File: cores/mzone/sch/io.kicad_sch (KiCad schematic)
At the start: 88 parts, among them SW3 SW_DIP_x06

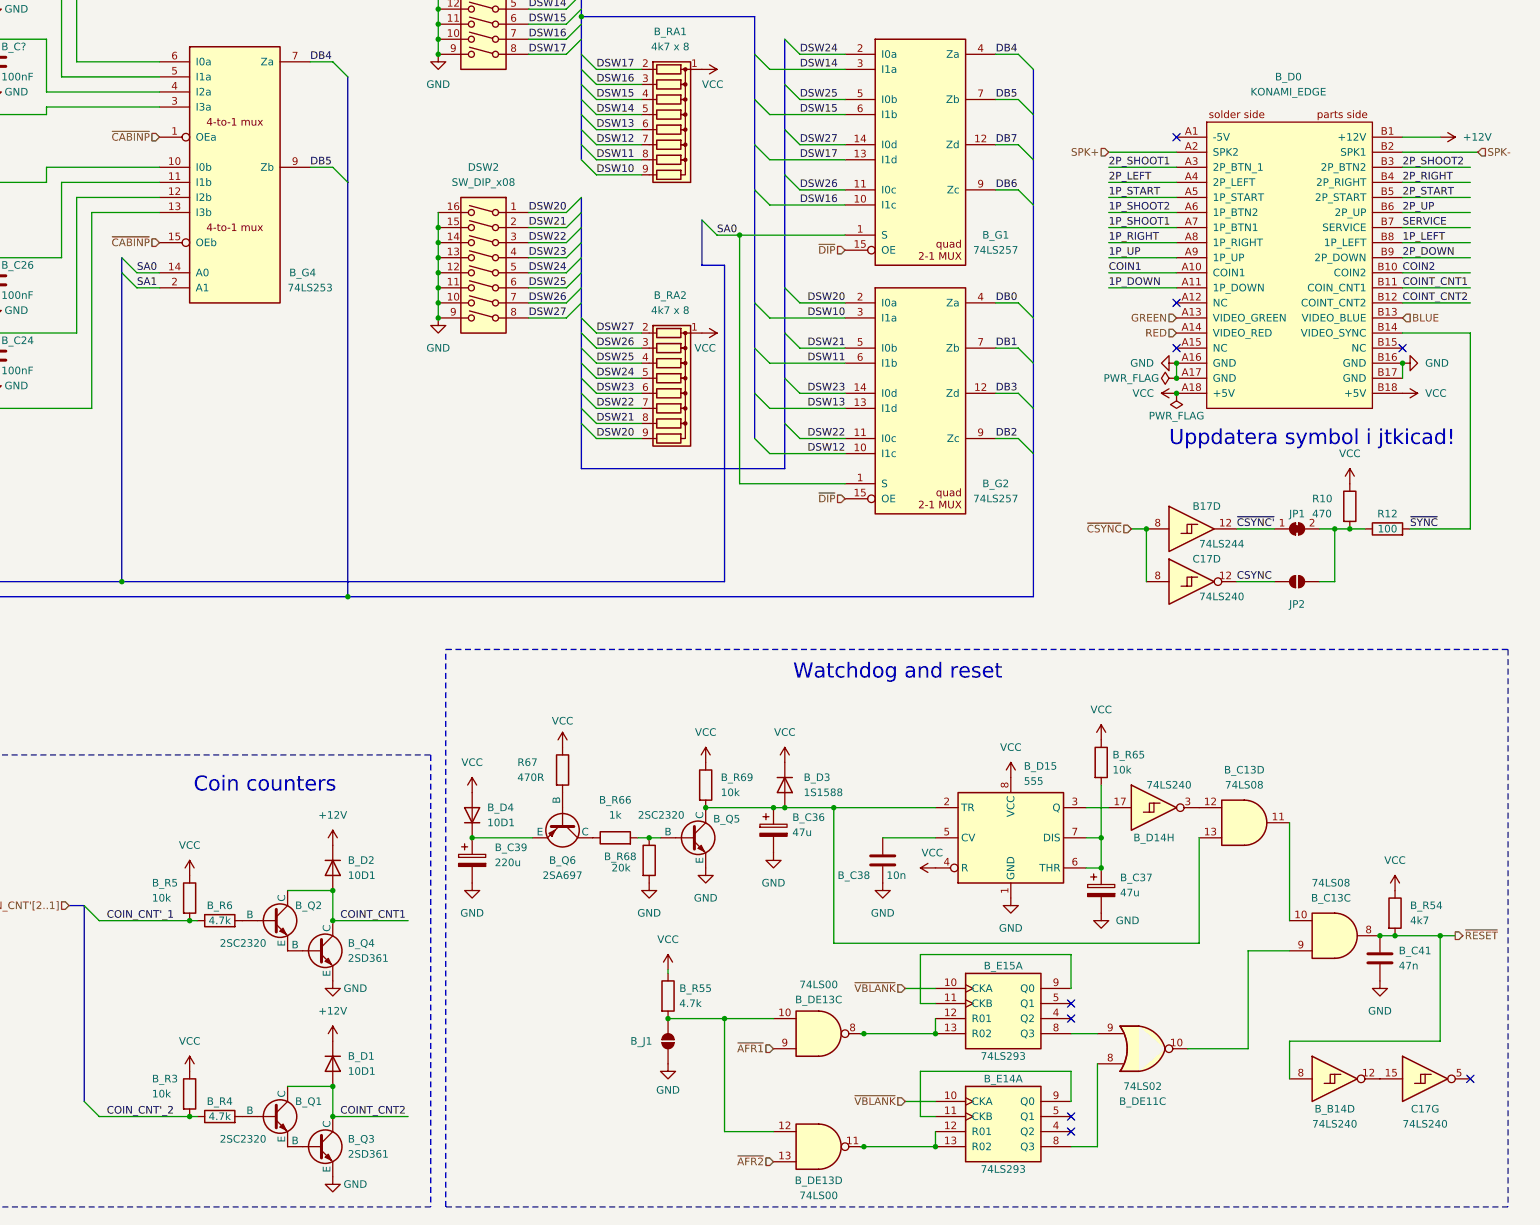
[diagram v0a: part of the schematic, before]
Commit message: mzone core
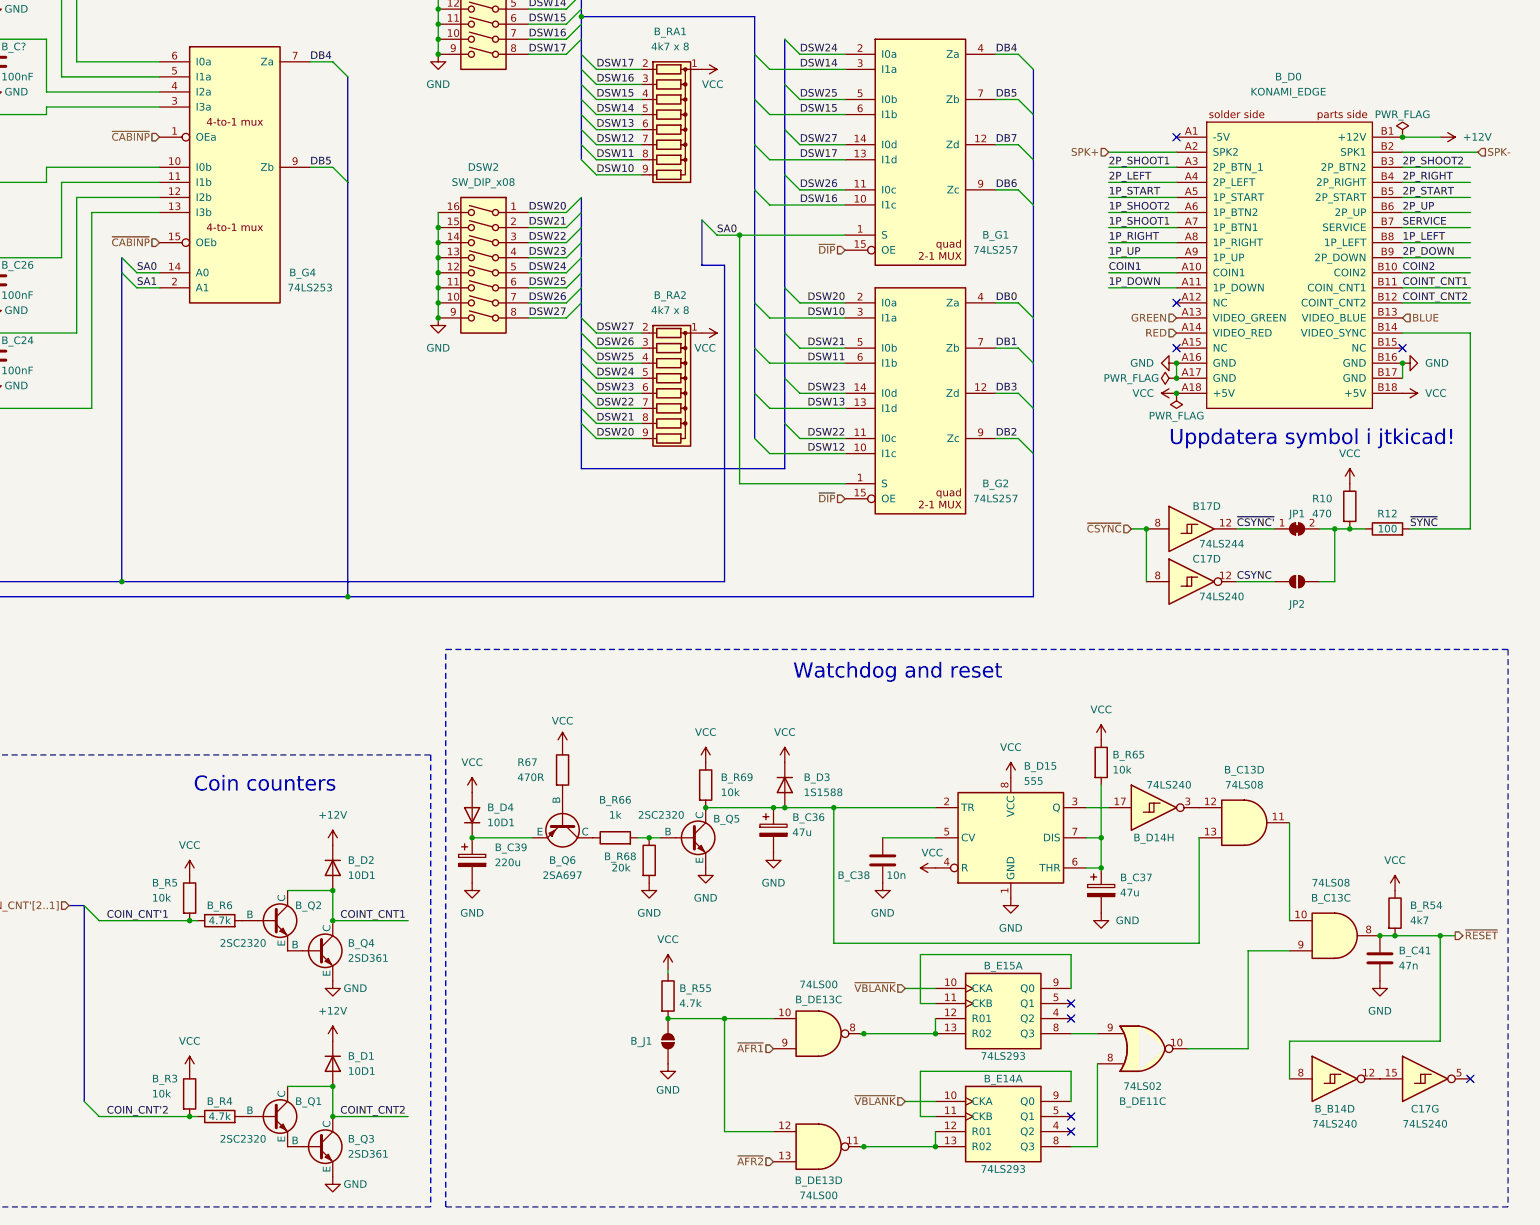
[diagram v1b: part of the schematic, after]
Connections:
- net COIN_CNT'_1 renamed COIN_CNT'1
- net COIN_CNT'_2 renamed COIN_CNT'2

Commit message: mzone core
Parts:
- gave numbers to parts that had none: 3
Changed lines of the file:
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@@
 		(on_board yes)
 		(dnp no)
-		(property "Reference" "B_R?"
+		(property "Reference" "B_R21"
 			(at 130.81 36.83 90)
 			(effects
@@
 			(project "megazone"
 				(path "/b3e039a8-74b0-4cb4-b612-5df1f0b42747/fc0cdb6a-9224-4695-8376-e66e14e5242d"
-					(reference "B_R?")
+					(reference "B_R21")
 					(unit 1)
 				)
@@
 		(on_board yes)
 		(dnp no)
-		(property "Reference" "B_R?"
+		(property "Reference" "B_R19"
 			(at 130.81 50.8 90)
 			(effects
@@
 			(project "megazone"
 				(path "/b3e039a8-74b0-4cb4-b612-5df1f0b42747/fc0cdb6a-9224-4695-8376-e66e14e5242d"
-					(reference "B_R?")
+					(reference "B_R19")
 					(unit 1)
 				)
@@
 		(on_board yes)
 		(dnp no)
-		(property "Reference" "B_R?"
+		(property "Reference" "B_R23"
 			(at 130.81 24.13 90)
 			(effects
@@
 			(project "megazone"
 				(path "/b3e039a8-74b0-4cb4-b612-5df1f0b42747/fc0cdb6a-9224-4695-8376-e66e14e5242d"
-					(reference "B_R?")
+					(reference "B_R23")
 					(unit 1)
 				)

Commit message: mzone core
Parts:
- added unit 2 of B_E4
- added unit 2 of B_F4
- added unit 2 of B_G4
- gave numbers to parts that had none: 3
- renumbered B_C11 to B_CC11, B_C12 to B_CC12, B_C13 to B_CC13, B_D4 to B_DD4, R10 to B_R10, R12 to B_R12, R14 to B_R14
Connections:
- net GND: now also B_E4.8 (GND), B_F4.8 (GND), B_G4.8 (GND)
- net VCC: now also B_E4.16 (VCC), B_F4.16 (VCC), B_G4.16 (VCC); no longer B_E4.16 (VCC), B_F4.16 (VCC), B_G4.16 (VCC)
- removed net VSS: B_E4.8 (VSS), B_F4.8 (VSS), B_G4.8 (VSS)

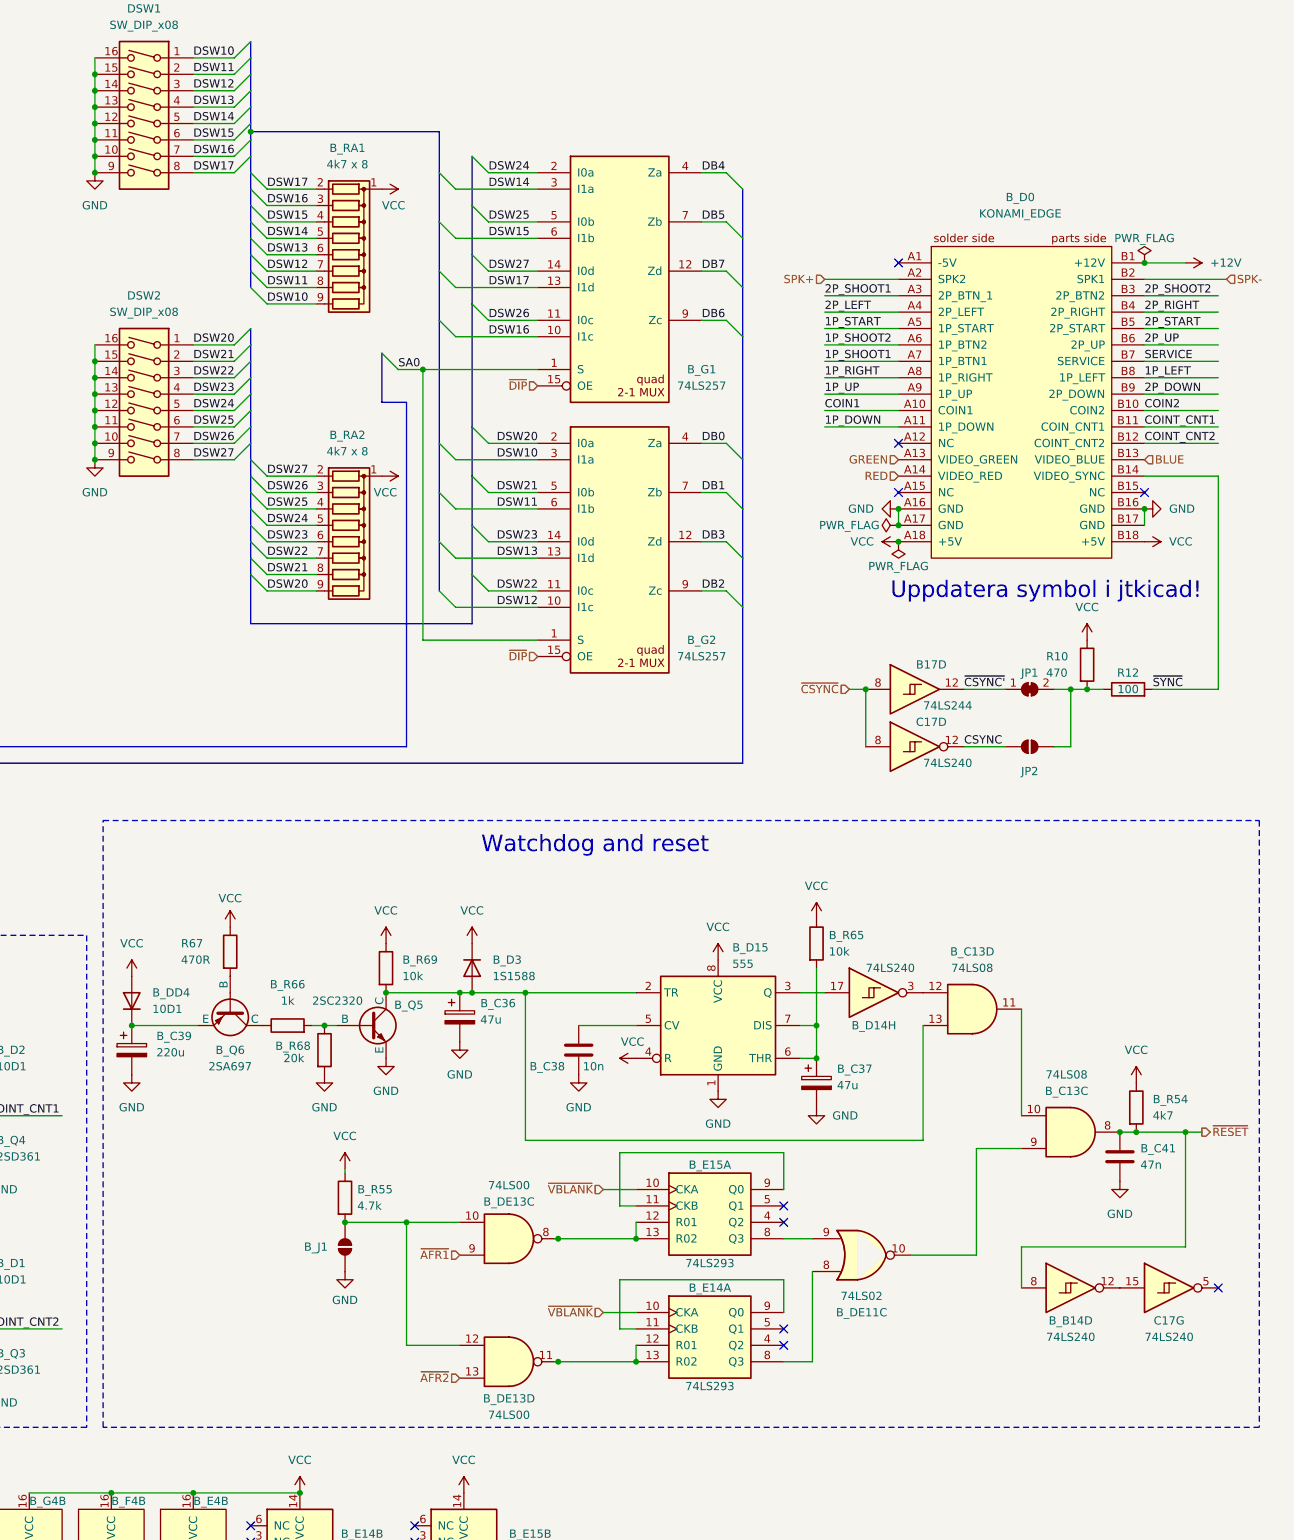
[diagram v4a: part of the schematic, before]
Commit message: mzone core
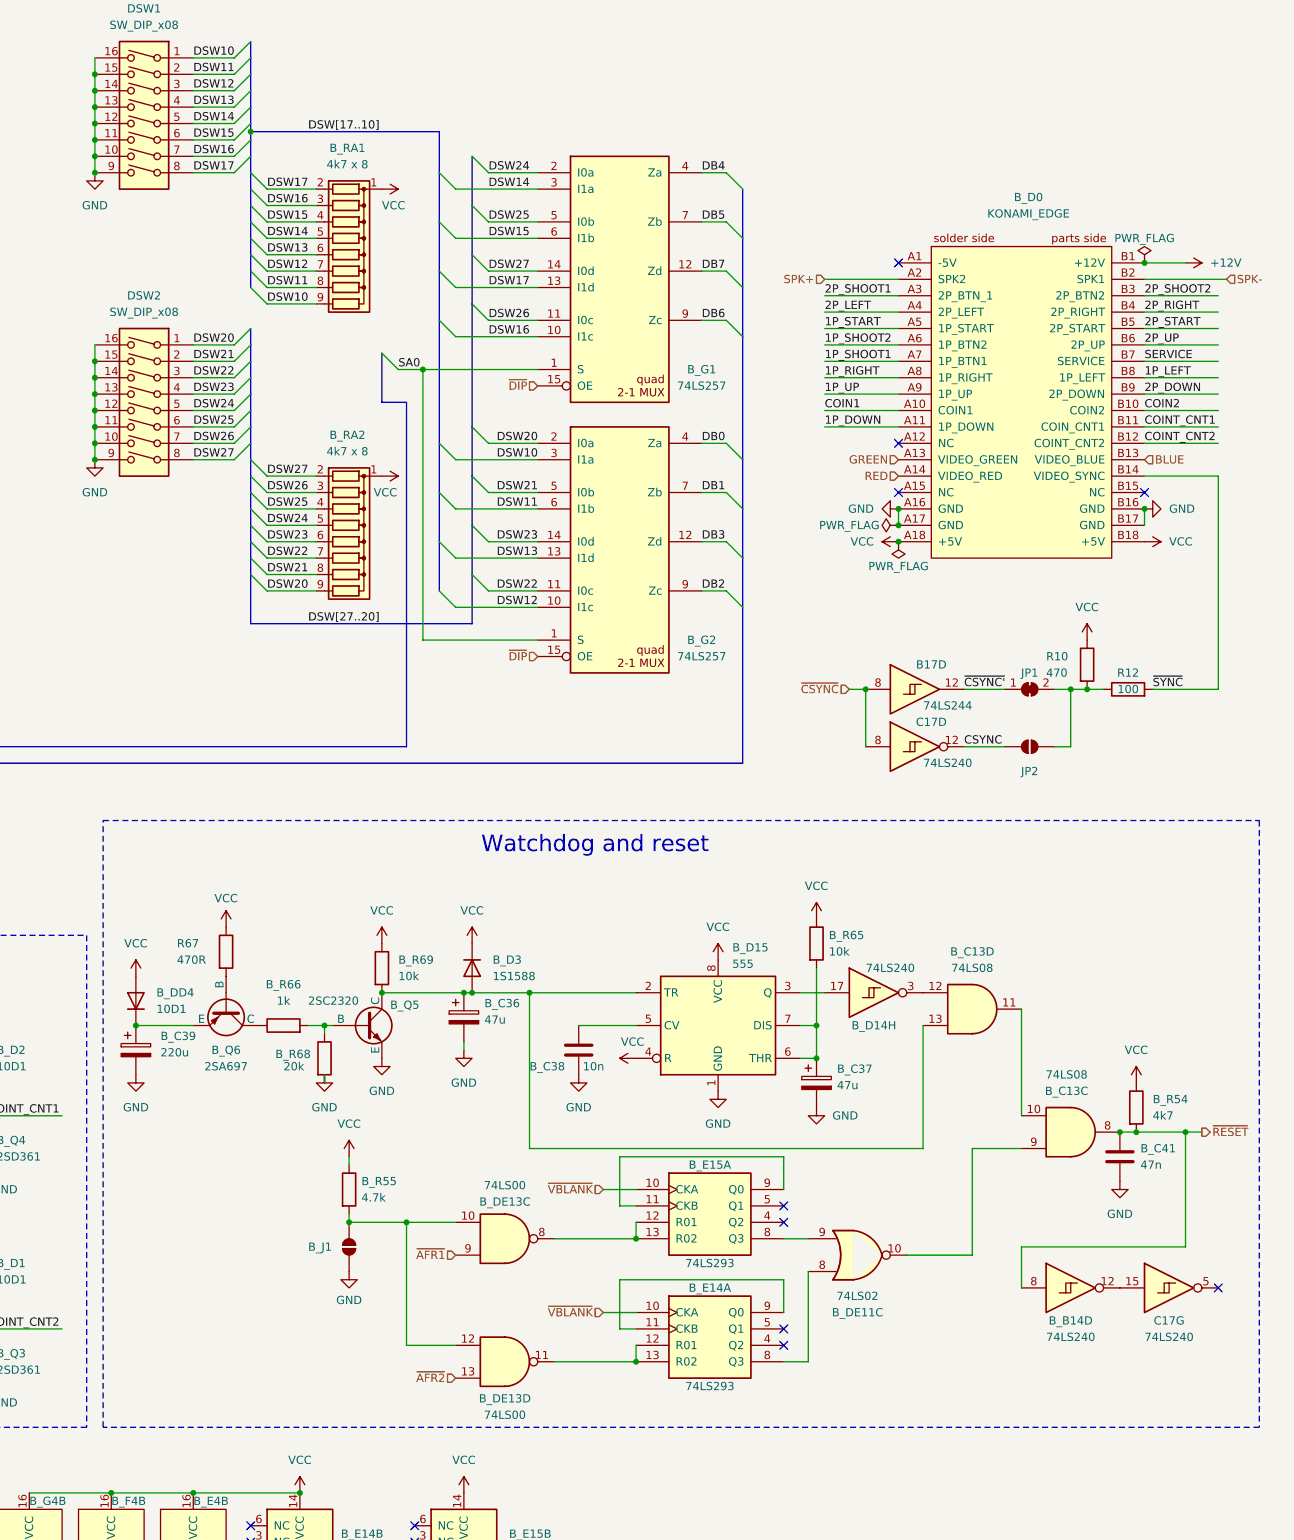
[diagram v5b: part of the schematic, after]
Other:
- note removed: "Uppdatera symbol i jtkicad!"
- company: (none) -> Konami GX319
- title: (none) -> Megazone
- moved on the sheet: B_C36, B_C39, B_DD4, B_DE11C, B_DE13C, B_DE13D, B_J1, B_Q5, B_Q6, B_R55, B_R66, B_R68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
